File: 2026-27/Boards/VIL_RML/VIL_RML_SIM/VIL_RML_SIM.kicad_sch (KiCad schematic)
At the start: 27 parts, among them J1 043045-0412, Q2 AO3401A, Q3 UJ3N065080K3S, Q4 AO3401A, U1 H11L1M, U2 NE555D

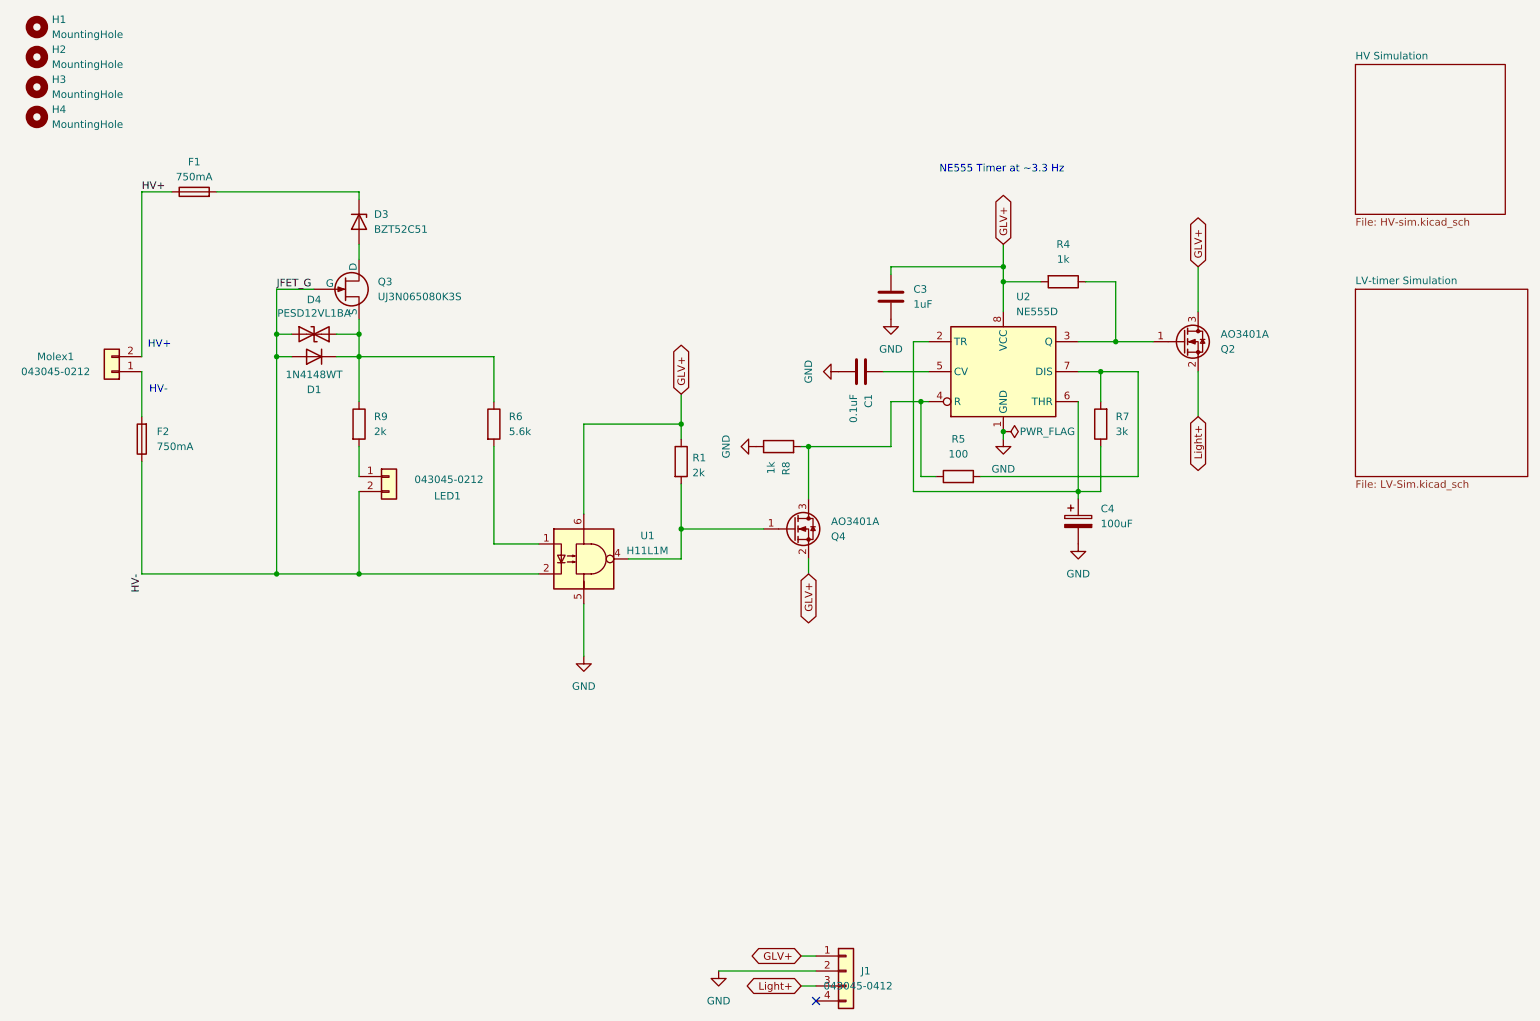
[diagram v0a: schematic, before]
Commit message: Updated VIL-RML Simulation
There is actually a square wave in the simulation now.

Also organized the folders a little better.
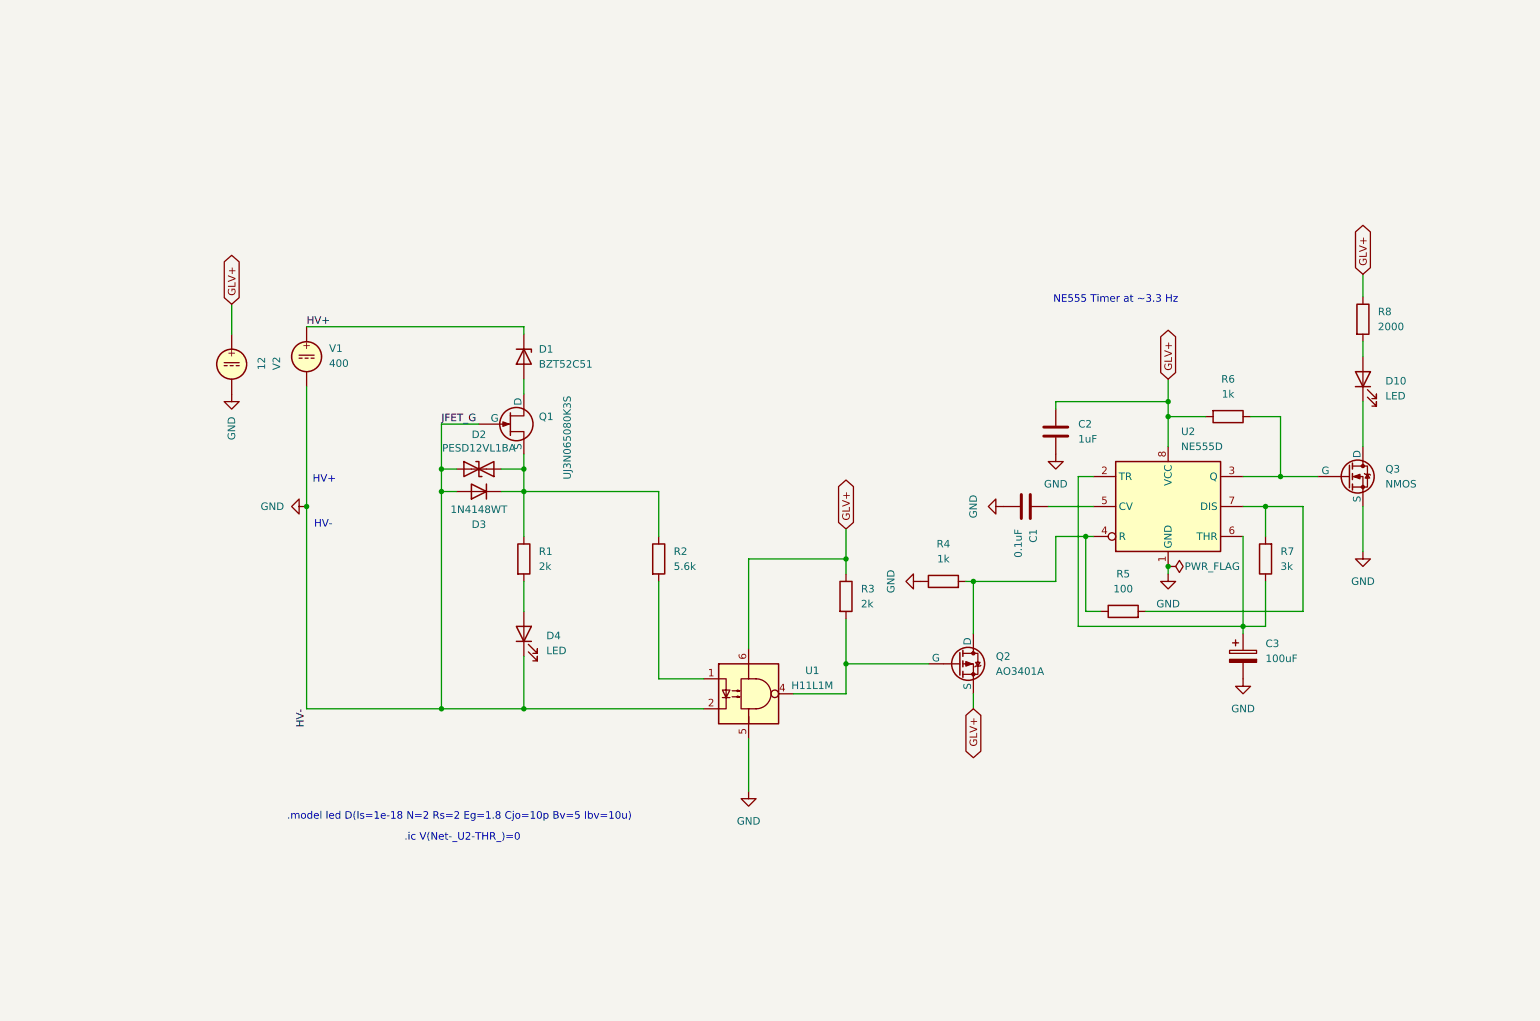
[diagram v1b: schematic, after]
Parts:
- removed C3: 1uF, Capacitor_SMD:C_0805_2012Metric_Pad1.18x1.45mm_HandSolder, symbol Device:C
- removed C4: 100uF, Capacitor_SMD:CP_Elec_6.3x5.4, symbol Device:C_Polarized
- removed D1: 1N4148WT, Diode_SMD:D_SOD-523, symbol Diode:1N4148WT
- removed D3: BZT52C51, Diode_SMD:D_SOD-123F, symbol Diode:BZT52Bxx
- removed D4: PESD12VL1BA, Diode_SMD:D_SOD-323, symbol Diode:1.5KExxCA
- removed F1, F2: 750mA, Fuse:Fuse_1206_3216Metric, symbol Device:Fuse
- removed H1, H2, H3, H4: MountingHole, MountingHole:MountingHole_3.2mm_M3, symbol Mechanical:MountingHole
- removed J1: 043045-0412, Connector_Molex:Molex_Micro-Fit_3.0_43045-0412_2x02_P3.00mm_Vertical, symbol Connector_Generic:Conn_01x04
- removed LED1, Molex1: 043045-0212, Connector_Molex:Molex_Micro-Fit_3.0_43045-0212_2x01_P3.00mm_Vertical, symbol Connector_Generic:Conn_01x02
- removed Q2, Q4: AO3401A, Package_TO_SOT_SMD:SOT-23, symbol Transistor_FET:AO3400A
- removed Q3: UJ3N065080K3S, Package_TO_SOT_THT:TO-247-3_Horizontal_TabDown, symbol Simulation_SPICE:NJFET
- removed R9: 2k, Resistor_SMD:R_0805_2012Metric_Pad1.20x1.40mm_HandSolder, symbol Device:R
- added C2: 1uF, Capacitor_SMD:C_0805_2012Metric_Pad1.18x1.45mm_HandSolder, symbol Device:C
- added C3: 100uF, Capacitor_SMD:CP_Elec_6.3x5.4, symbol Device:C_Polarized
- added D1: BZT52C51, Diode_SMD:D_SOD-123F, symbol Diode:BZT52Bxx
- added D10, D4: LED, symbol Device:LED
- added D2: PESD12VL1BA, Diode_SMD:D_SOD-323, symbol Diode:1.5KExxCA
- added D3: 1N4148WT, Diode_SMD:D_SOD-523, symbol Diode:1N4148WT
- added Q1: UJ3N065080K3S, Package_TO_SOT_THT:TO-247-3_Horizontal_TabDown, symbol Simulation_SPICE:NJFET
- added Q2: AO3401A, Package_TO_SOT_SMD:SOT-23, symbol Simulation_SPICE:PMOS
- added Q3: NMOS, symbol Simulation_SPICE:NMOS
- added R2: 5.6k, Resistor_SMD:R_0805_2012Metric_Pad1.20x1.40mm_HandSolder, symbol Device:R
- added R3: 2k, Resistor_SMD:R_0805_2012Metric_Pad1.20x1.40mm_HandSolder, symbol Device:R
- added V1: 400, symbol Simulation_SPICE:VDC
- added V2: 12, symbol Simulation_SPICE:VDC
- R6: value 5.6k -> 1k
- R8: value 1k -> 2000; now left out of the parts list
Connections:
- net HV- is gone; now on net GND: U1.2
- net GLV+: now also R6.2, R8.1, C2.2, Q2.3 (S), R3.1, V2.1; no longer R1.1, R4.2
- net GND: now also R4.1, C2.1, C3.2, D2.2 (A2), D3.2 (A), D4.1 (K), Q1.1 (G), Q3.3 (S), V1.2, V2.2; no longer R8.1
- net HV+: now also D1.1 (K), V1.1
- net at R7.1, U2.2 (TR), U2.6 (THR): now also C3.1
- net at U2.3 (Q): now also R6.1, Q3.2 (G); no longer R4.1
- net at R5.1, U2.4 (R): now also R4.2, Q2.1 (D); no longer R8.2
- net at R1.2: now also D4.2 (A); no longer U1.4
- net at U1.1: now also R2.2; no longer R6.2
- new net: D2.1 (A1), D3.1 (K), Q1.3 (S), R1.1, R2.1
- new net: Q2.2 (G), R3.2, U1.4
- new net: D10.1 (K), Q3.1 (D)
- new net: D10.2 (A), R8.2
- new net: D1.2 (A), Q1.2 (D)
- no-connect marks 1 -> 0
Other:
- removed sheet HV Simulation
- removed sheet LV-timer Simulation
- note added: ".ic V(Net-_U2-THR_)=0"
- note added: ".model led D(Is=1e-18 N=2 Rs=2 Eg=1.8 Cjo=10p Bv=5 Ibv=10u)"
